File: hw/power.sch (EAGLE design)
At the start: 92 parts, among them SW1 MF-SW-TACT-4.2MM, SW2 MF-SW-TACT-4.2MM, U1 TPS54200, U2 TPS54200, U3 TPS54200, U4 TPS54200, U5 MIC280, U6 MIC280, U7 MIC5233, U8 NRF52832, Y1 32MHz, Y2 32.768kHz

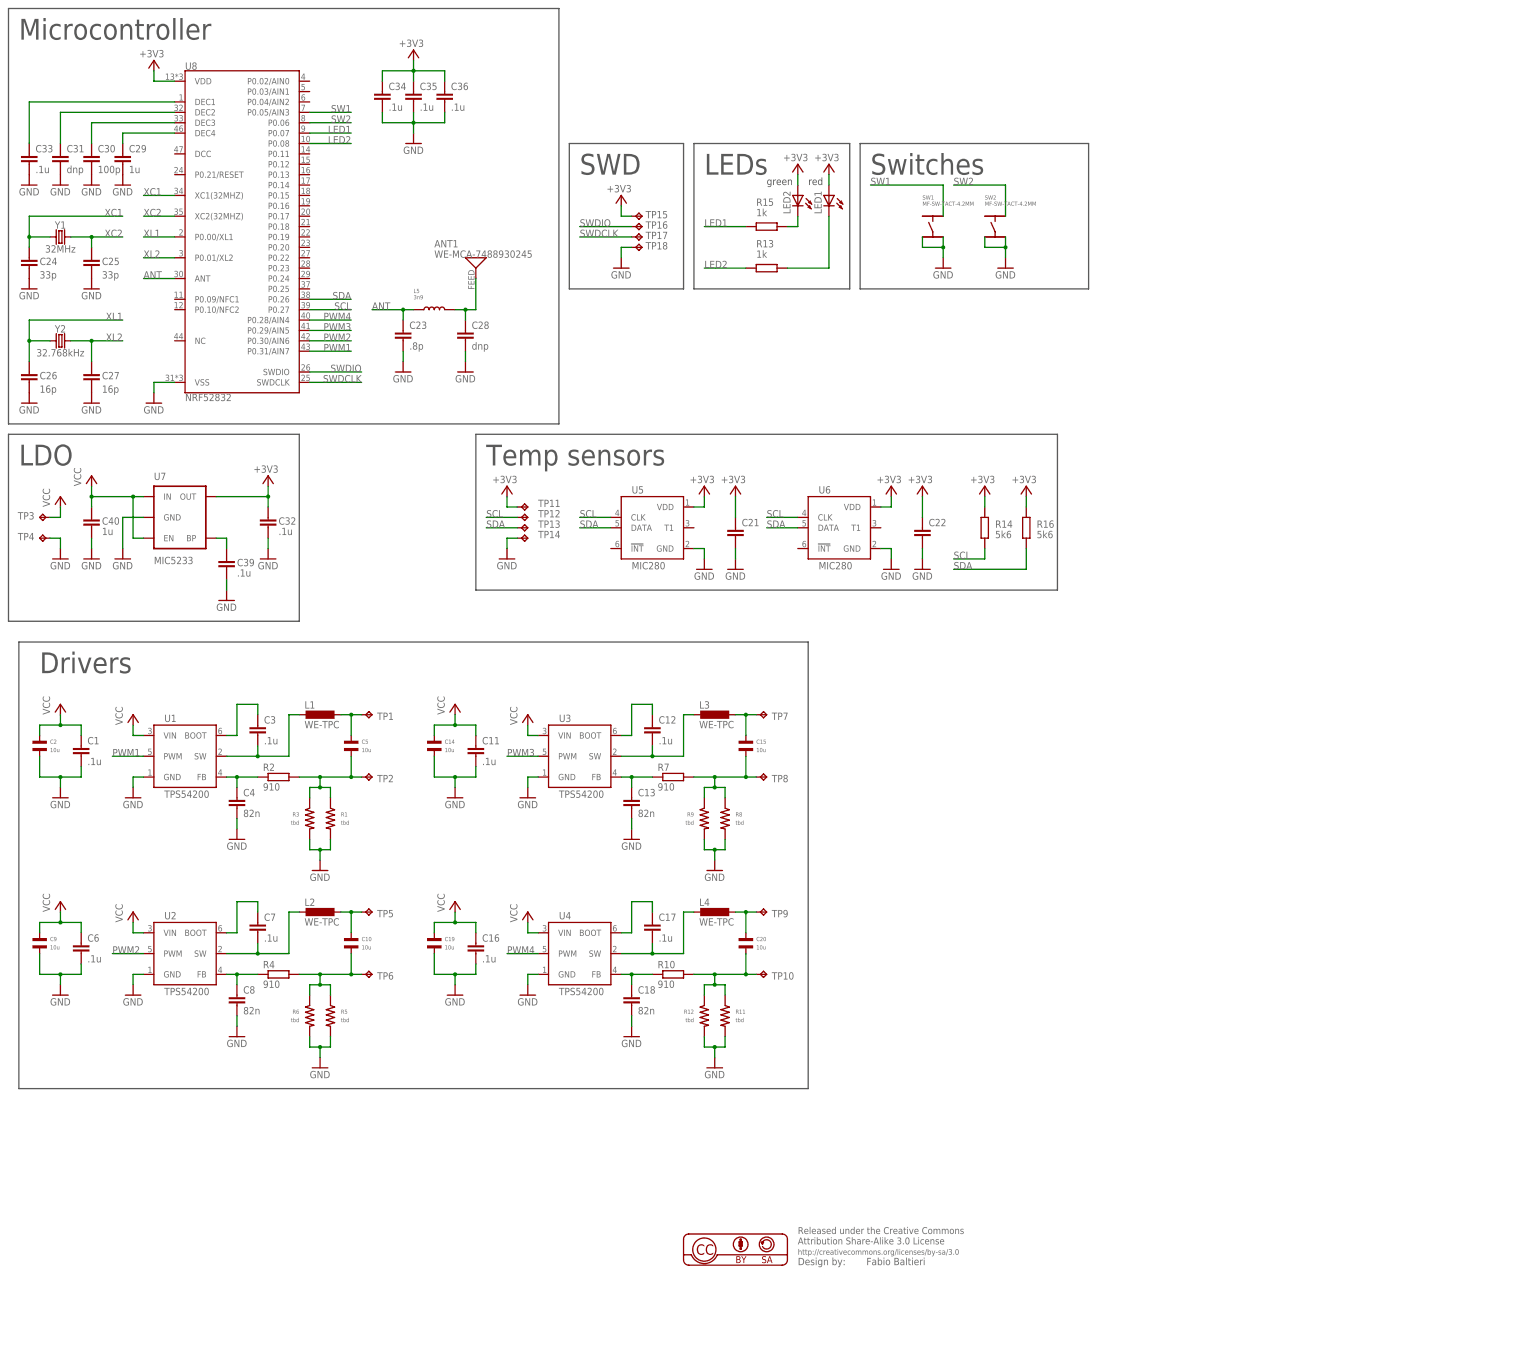
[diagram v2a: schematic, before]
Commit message: power: schematic refactoring?
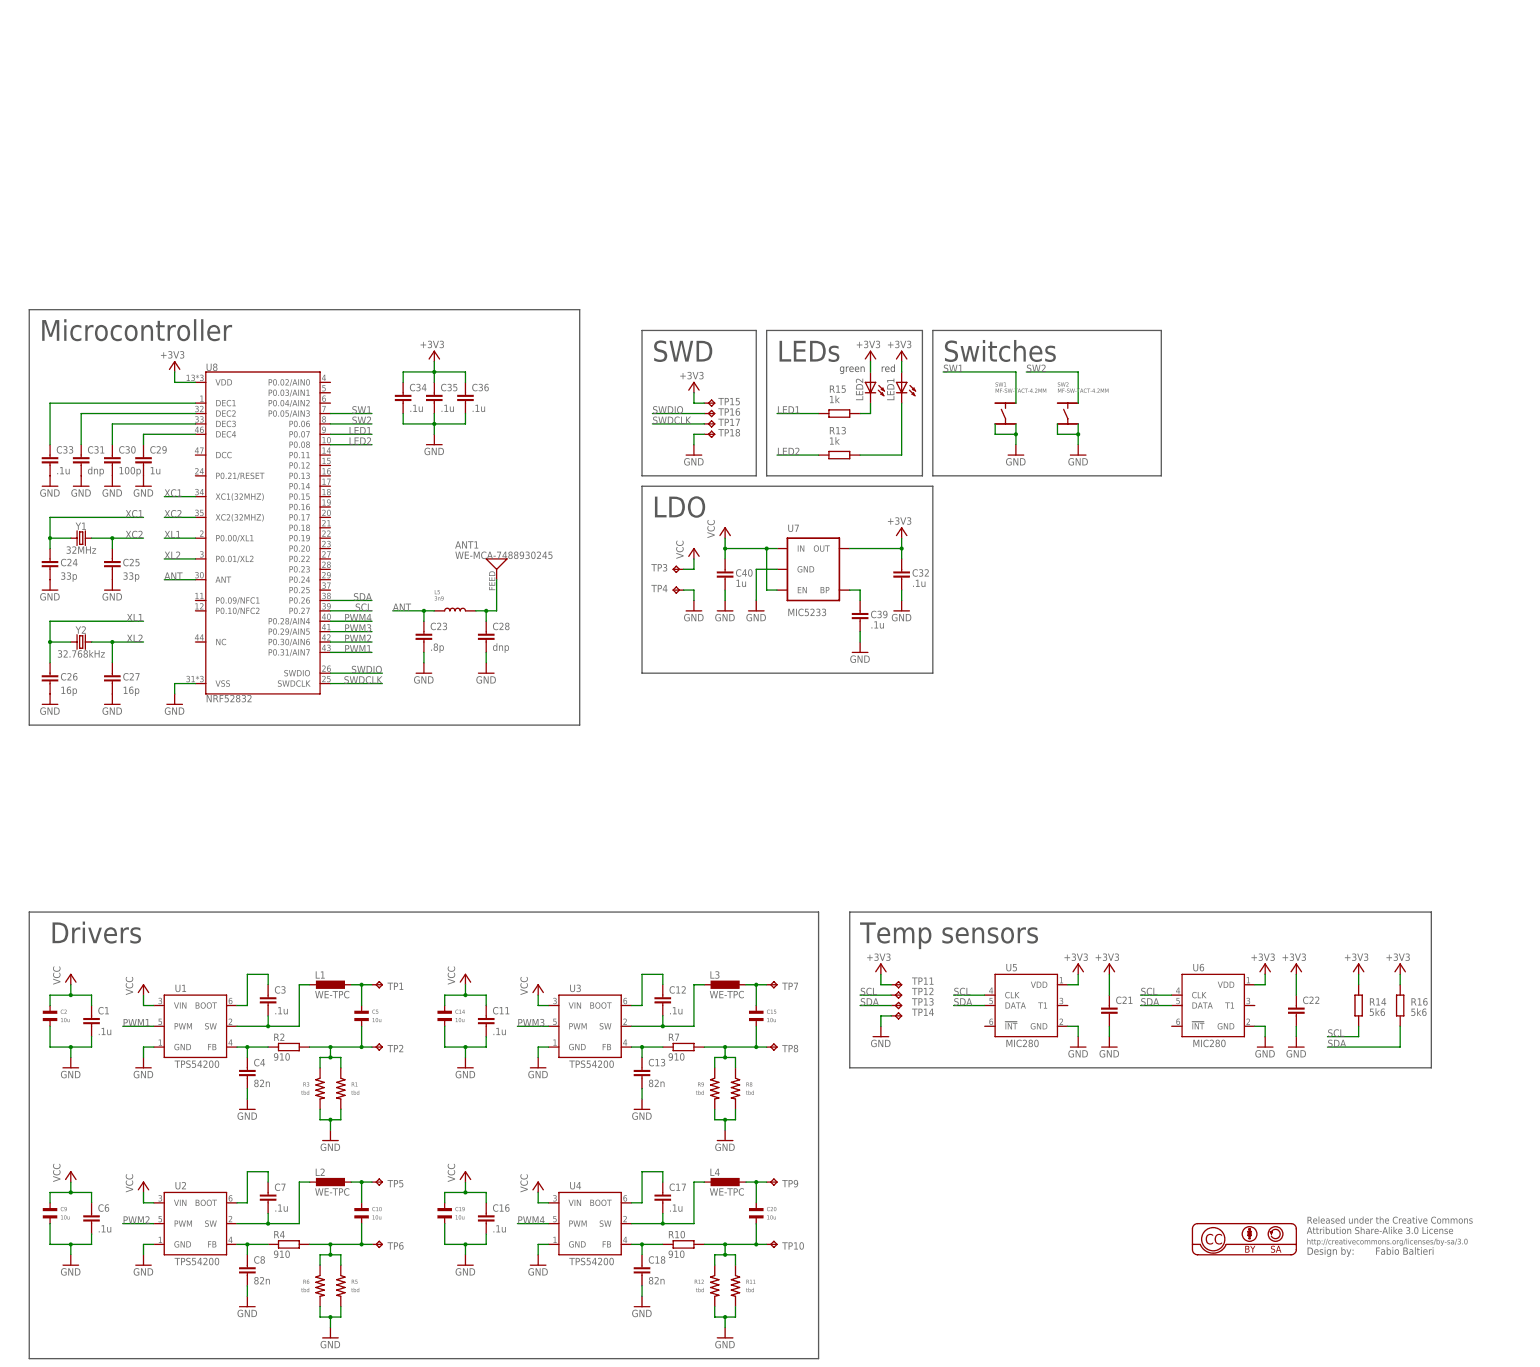
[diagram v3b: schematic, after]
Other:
- moved on the sheet: ANT1, C1, C10, C11, C12, C13, C14, C15, C16, C17, C18, C19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

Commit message: power: few assembly notes
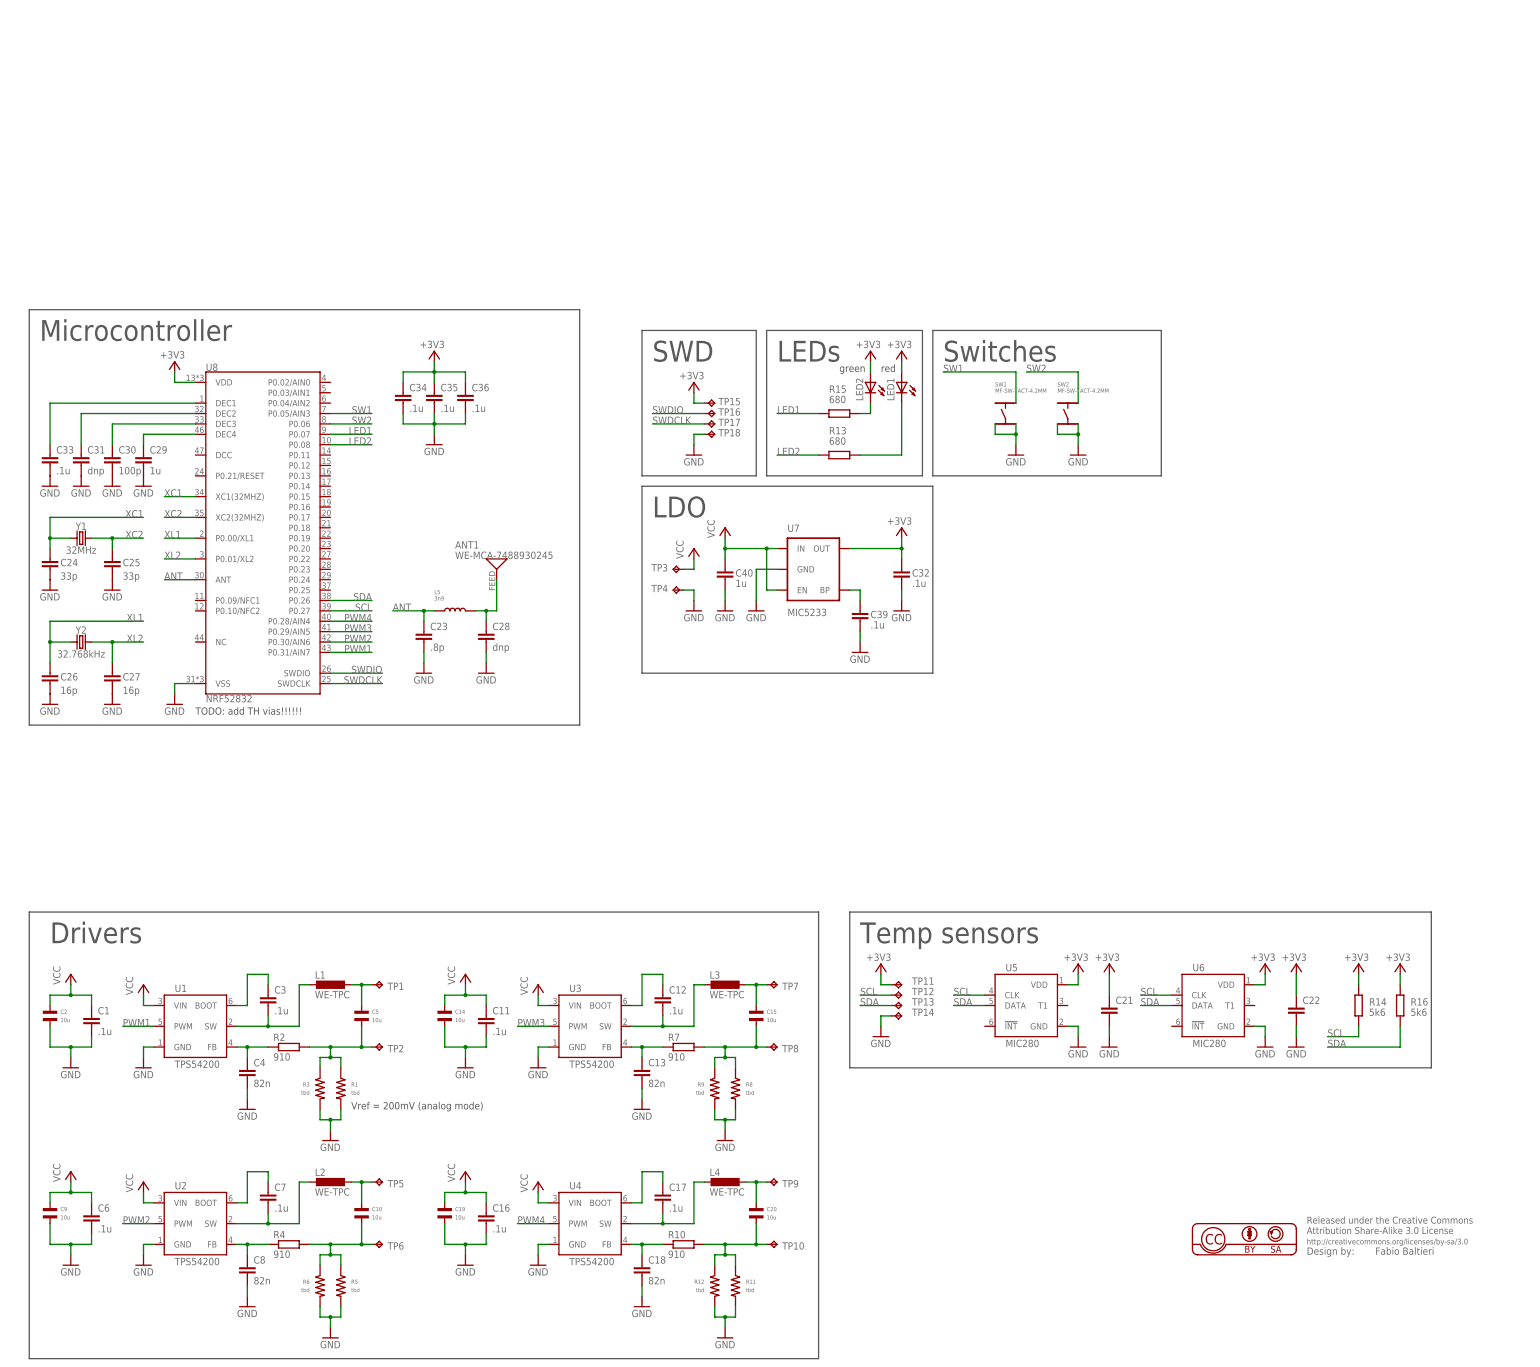
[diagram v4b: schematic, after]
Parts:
- R13, R15: value 1k -> 680
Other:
- note added: "TODO: add TH vias!!!!!!"
- note added: "Vref = 200mV (analog mode)"

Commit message: hw: add few assembly notes and values
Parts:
- R1, R11, R12, R3, R5, R6, R8, R9: value tbd -> 270
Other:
- note added: "TODO Add TH vias!!!!!! Battery measurement TP and connector labels New temperature sensor (TP100?) Power cable strain relief holes"
- note added: "i2c addr = 0x48"
- note added: "i2c addr = 0x49"
- note removed: "TODO: add TH vias!!!!!!"
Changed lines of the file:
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@@
 <part name="P+3" library="supply1" deviceset="VCC" device=""/>
 <part name="GND5" library="supply1" deviceset="GND" device=""/>
-<part name="R1" library="MF_Passives" deviceset="RESISTOR" device="_0805" value="tbd"/>
-<part name="R3" library="MF_Passives" deviceset="RESISTOR" device="_0805" value="tbd"/>
+<part name="R1" library="MF_Passives" deviceset="RESISTOR" device="_0805" value="270"/>
+<part name="R3" library="MF_Passives" deviceset="RESISTOR" device="_0805" value="270"/>
 <part name="P+4" library="supply1" library_urn="urn:adsk.eagle:library:371" deviceset="VCC" device=""/>
 <part name="GND6" library="supply1" library_urn="urn:adsk.eagle:library:371" deviceset="GND" device=""/>
@@
 <part name="C9" library="MF_Passives" deviceset="CAPACITOR_NP" device="_1206" value="10u"/>
 <part name="C10" library="MF_Passives" deviceset="CAPACITOR_NP" device="_1206" value="10u"/>
-<part name="R5" library="MF_Passives" deviceset="RESISTOR" device="_0805" value="tbd"/>
-<part name="R6" library="MF_Passives" deviceset="RESISTOR" device="_0805" value="tbd"/>
+<part name="R5" library="MF_Passives" deviceset="RESISTOR" device="_0805" value="270"/>
+<part name="R6" library="MF_Passives" deviceset="RESISTOR" device="_0805" value="270"/>
 <part name="P+6" library="supply1" library_urn="urn:adsk.eagle:library:371" deviceset="VCC" device=""/>
 <part name="GND10" library="supply1" library_urn="urn:adsk.eagle:library:371" deviceset="GND" device=""/>
@@
 <part name="C14" library="MF_Passives" deviceset="CAPACITOR_NP" device="_1206" value="10u"/>
 <part name="C15" library="MF_Passives" deviceset="CAPACITOR_NP" device="_1206" value="10u"/>
-<part name="R8" library="MF_Passives" deviceset="RESISTOR" device="_0805" value="tbd"/>
-<part name="R9" library="MF_Passives" deviceset="RESISTOR" device="_0805" value="tbd"/>
+<part name="R8" library="MF_Passives" deviceset="RESISTOR" device="_0805" value="270"/>
+<part name="R9" library="MF_Passives" deviceset="RESISTOR" device="_0805" value="270"/>
 <part name="P+8" library="supply1" library_urn="urn:adsk.eagle:library:371" deviceset="VCC" device=""/>
 <part name="GND14" library="supply1" library_urn="urn:adsk.eagle:library:371" deviceset="GND" device=""/>
@@
 <part name="C19" library="MF_Passives" deviceset="CAPACITOR_NP" device="_1206" value="10u"/>
 <part name="C20" library="MF_Passives" deviceset="CAPACITOR_NP" device="_1206" value="10u"/>
-<part name="R11" library="MF_Passives" deviceset="RESISTOR" device="_0805" value="tbd"/>
-<part name="R12" library="MF_Passives" deviceset="RESISTOR" device="_0805" value="tbd"/>
+<part name="R11" library="MF_Passives" deviceset="RESISTOR" device="_0805" value="270"/>
+<part name="R12" library="MF_Passives" deviceset="RESISTOR" device="_0805" value="270"/>
 <part name="U5" library="balto" deviceset="MIC280" device=""/>
 <part name="U6" library="balto" deviceset="MIC280" device=""/>
@@
 <text x="203.2" y="243.84" size="1.778" layer="97">green</text>
 <text x="83.82" y="63.5" size="1.778" layer="97">Vref = 200mV (analog mode)</text>
-<text x="45.72" y="160.02" size="1.778" layer="97">TODO: add TH vias!!!!!!</text>
+<text x="48.26" y="137.16" size="1.778" layer="97">TODO
+Add TH vias!!!!!!
+Battery measurement
+TP and connector labels
+New temperature sensor (TP100?)
+Power cable strain relief holes</text>
+<text x="238.76" y="76.2" size="1.778" layer="97">i2c addr = 0x48</text>
+<text x="284.48" y="76.2" size="1.778" layer="97">i2c addr = 0x49</text>
 </plain>
 <instances>
@@
 </drawing>
 <compatibility>
+<note version="6.3" minversion="6.2.2" severity="warning">
+Since Version 6.2.2 text objects can contain more than one line,
+which will not be processed correctly with this version.
+</note>
 <note version="8.2" severity="warning">
 Since Version 8.2, EAGLE supports online libraries. The ids
